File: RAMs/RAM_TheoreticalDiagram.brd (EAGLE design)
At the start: 229.5 x 172.7 mm, 23 parts, among them IC1 74HC573D, IC10 74HC573D, IC11 74HC573D, IC12 74HC573D, IC13 74HC573D, IC14 74HC573D, IC15 74HC573D, IC16 74HC573D, IC17 74HC154DW, IC18 74HC154DW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

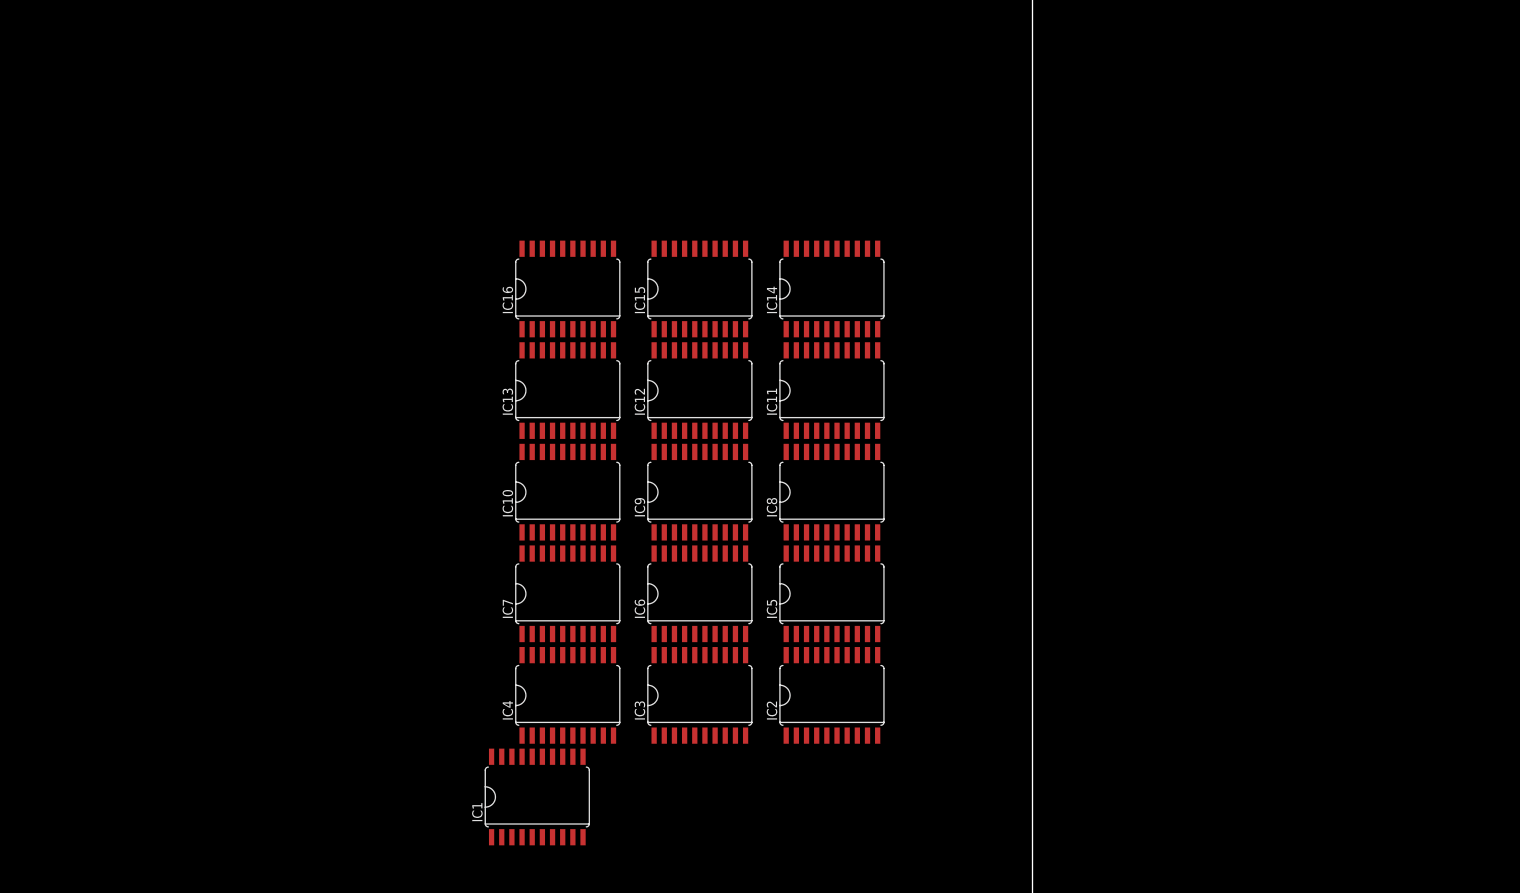
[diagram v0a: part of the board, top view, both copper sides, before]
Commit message: Finished the RAM boards
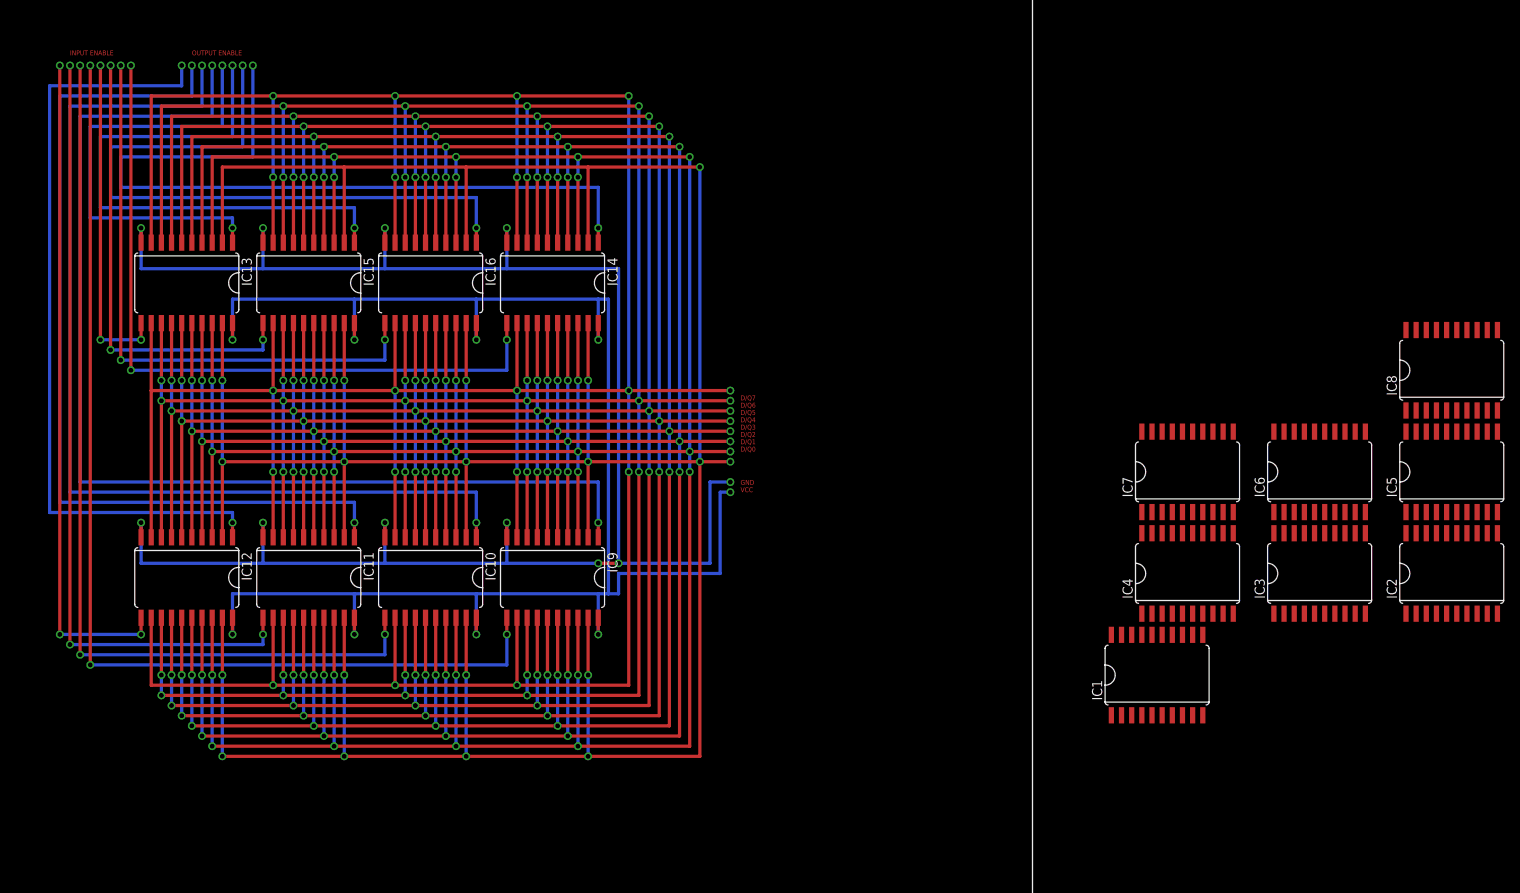
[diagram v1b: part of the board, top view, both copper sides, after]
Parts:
- moved IC1 79.0 mm to (245.1, 77.5)
- moved IC2 79.0 mm to (281.9, 90.2)
- moved IC3 79.0 mm to (265.4, 90.2)
- moved IC4 79.0 mm to (248.9, 90.2)
- moved IC5 79.0 mm to (281.9, 102.9)
- moved IC6 79.0 mm to (265.4, 102.9)
- moved IC7 79.0 mm to (248.9, 102.9)
- moved IC8 79.0 mm to (281.9, 115.6)
- moved IC11 69.5 mm to (139.1, 89.7), turned to 180 degrees
- moved IC12 68.3 mm to (123.8, 89.7), turned to 180 degrees
- moved IC13 49.5 mm to (123.8, 126.5), turned to 180 degrees
- moved IC15 48.9 mm to (139.1, 126.5), turned to 180 degrees
- moved IC14 34.9 mm to (169.5, 126.5), turned to 180 degrees
- moved IC9 21.3 mm to (169.5, 89.7), turned to 180 degrees
- moved IC10 20.2 mm to (154.3, 89.7), turned to 180 degrees
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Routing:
- net N$135: track 0.00 -> 468.6 mm, vias 0 -> 19
- net N$171: track 0.00 -> 467.4 mm, vias 0 -> 29
- net N$180: track 0.00 -> 466.1 mm, vias 0 -> 29
- net N$156: track 0.00 -> 464.8 mm, vias 0 -> 29
- net N$182: track 0.00 -> 463.5 mm, vias 0 -> 29
- net N$148: track 0.00 -> 462.3 mm, vias 0 -> 29
- net N$184: track 0.00 -> 461.0 mm, vias 0 -> 29
- net N$199: track 0.00 -> 459.7 mm, vias 0 -> 19
- net N$151: track 0.00 -> 231.1 mm, vias 0 -> 11
- net N$144: track 0.00 -> 209.6 mm, vias 0 -> 9
- net N$149: track 0.00 -> 139.7 mm, vias 0 -> 2
- net N$143: track 0.00 -> 132.1 mm, vias 0 -> 3
- net N$136: track 0.00 -> 125.7 mm, vias 0 -> 2
- net N$145: track 0.00 -> 115.6 mm, vias 0 -> 3
- net N$132: track 0.00 -> 111.8 mm, vias 0 -> 2
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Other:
- board text added: "D/Q7 D/Q6 D/Q5 D/Q4 D/Q3 D/Q2 D/Q1 D/Q0"
- board text added: "GND VCC"
- board text added: "INPUT ENABLE"
- board text added: "OUTPUT ENABLE"

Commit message: Changed the dimension of the board a bit
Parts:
- moved IC2 231.4 mm to (64.8, 10.2)
- moved IC3 231.4 mm to (48.3, 10.2)
- moved IC5 231.4 mm to (64.8, 22.9)
- moved IC6 231.4 mm to (48.3, 22.9)
- moved IC8 231.4 mm to (64.8, 35.6)
- moved IC4 231.4 mm to (31.8, 10.2)
- moved IC7 231.4 mm to (31.8, 22.9)
- moved IC1 201.3 mm to (48.3, 35.6)
- moved IC12 51.2 mm to (103.5, 42.7)
- moved IC13 51.2 mm to (103.5, 79.5)
- moved IC10 51.2 mm to (134.0, 42.7)
- moved IC11 51.2 mm to (118.7, 42.7)
- moved IC14 51.2 mm to (149.2, 79.5)
- moved IC15 51.2 mm to (118.7, 79.5)
- moved IC16 51.2 mm to (134.0, 79.5)
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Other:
- board size 229.5 x 172.7 mm -> 177.5 x 111.8 mm
